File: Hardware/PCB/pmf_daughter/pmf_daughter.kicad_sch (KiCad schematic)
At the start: 40 parts, among them J1 Conn_02x07_Odd_Even

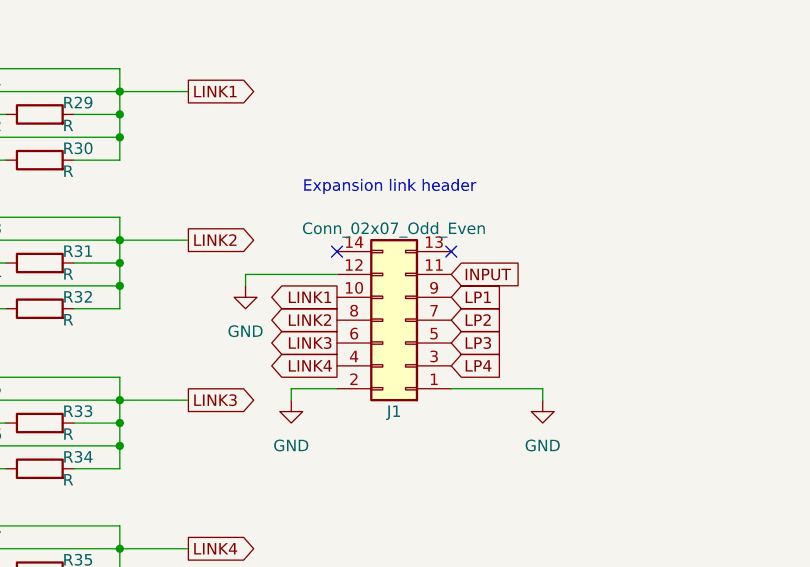
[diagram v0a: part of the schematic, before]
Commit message: Font change; GND instead of NC on d-board
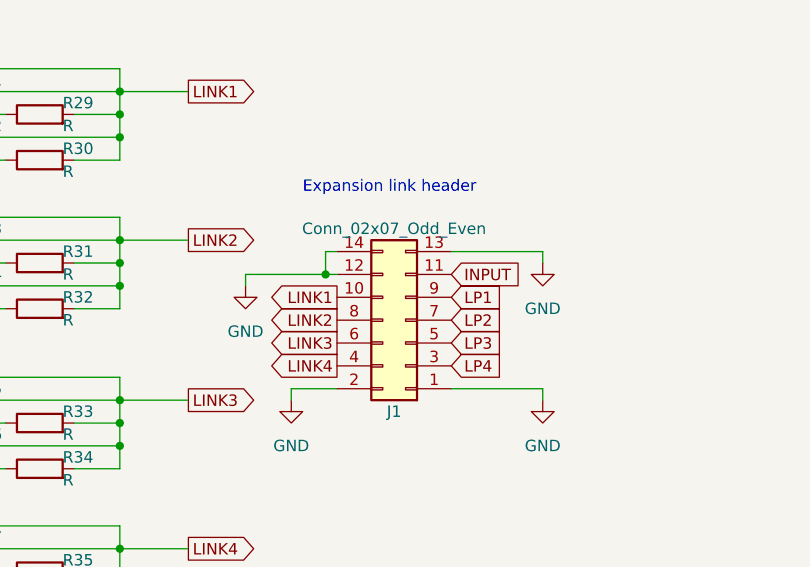
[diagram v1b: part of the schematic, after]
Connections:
- net GND: now also J1.13 (Pin_13), J1.14 (Pin_14)
- no-connect marks 2 -> 0
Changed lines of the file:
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@@
   (junction (at 154.94 66.04) (diameter 0) (color 0 0 0 0)
   )
+  (junction (at 177.8 81.28) (diameter 0) (color 0 0 0 0)
+  )
   (junction (at 154.94 111.76) (diameter 0) (color 0 0 0 0)
   )
   (junction (at 154.94 60.96) (diameter 0) (color 0 0 0 0)
   )
-  (no_connect (at 191.77 78.74))
-  (no_connect (at 179.07 78.74))
   (wire (pts (xy 109.22 92.71) (xy 154.94 92.71))
     (stroke (width 0) (type default))
@@
     (stroke (width 0) (type default))
   )
+  (wire (pts (xy 201.93 78.74) (xy 201.93 80.01))
+    (stroke (width 0) (type default))
+  )
   (wire (pts (xy 139.7 82.55) (xy 154.94 82.55))
     (stroke (width 0) (type default))
@@
     (stroke (width 0) (type default))
   )
+  (wire (pts (xy 177.8 81.28) (xy 177.8 78.74))
+    (stroke (width 0) (type default))
+  )
   (wire (pts (xy 154.94 60.96) (xy 162.56 60.96))
     (stroke (width 0) (type default))
@@
     (stroke (width 0) (type default))
   )
+  (wire (pts (xy 177.8 78.74) (xy 179.07 78.74))
+    (stroke (width 0) (type default))
+  )
   (wire (pts (xy 154.94 95.25) (xy 162.56 95.25))
     (stroke (width 0) (type default))
@@
     (stroke (width 0) (type default))
   )
+  (wire (pts (xy 168.91 81.28) (xy 177.8 81.28))
+    (stroke (width 0) (type default))
+  )
   (wire (pts (xy 168.91 82.55) (xy 168.91 81.28))
     (stroke (width 0) (type default))
@@
     (stroke (width 0) (type default))
   )
+  (wire (pts (xy 201.93 78.74) (xy 191.77 78.74))
+    (stroke (width 0) (type default))
+  )
   (wire (pts (xy 154.94 92.71) (xy 154.94 95.25))
     (stroke (width 0) (type default))
@@
     (stroke (width 0) (type default))
   )
-  (wire (pts (xy 168.91 81.28) (xy 179.07 81.28))
-    (stroke (width 0) (type default))
-  )
   (wire (pts (xy 149.86 80.01) (xy 154.94 80.01))
     (stroke (width 0) (type default))
@@
   )
   (wire (pts (xy 99.06 80.01) (xy 121.92 80.01))
+    (stroke (width 0) (type default))
+  )
+  (wire (pts (xy 177.8 81.28) (xy 179.07 81.28))
     (stroke (width 0) (type default))
   )
@@
         )
       )
+    )
+  )
+  (symbol (lib_id "power:GND") (at 201.93 80.01 0) (mirror y) (unit 1)
+    (in_bom yes) (on_board yes) (dnp no) (fields_autoplaced)
+    (property "Reference" "#PWR036" (at 201.93 86.36 0)
+      (effects (font (size 1.27 1.27)) hide)
+    )
+    (property "Value" "GND" (at 201.93 85.09 0)
+      (effects (font (size 1.27 1.27)))
+    )
+    (property "Footprint" "" (at 201.93 80.01 0)
+      (effects (font (size 1.27 1.27)) hide)
+    )
+    (property "Datasheet" "" (at 201.93 80.01 0)
+      (effects (font (size 1.27 1.27)) hide)
+    )
+    (pin "1")
+    (instances
+      (project "pmf_daughter"
+        (path "/1fce46f5-2003-4c7e-915f-b9b7dfc679d7"
+          (reference "#PWR036") (unit 1)
+        )
+      )
